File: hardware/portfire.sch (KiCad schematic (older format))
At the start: 31 parts, among them P101 1, P102 11, P103 2, P104 12, P105 3, P106 13, P107 4, P108 14, P109 5, P110 15, P111 6, P112 21, P113 7, P114 22, P115 8, P116 23, P117 9, P118 24, P119 10, P120 25, P121 16, P122 17, P123 18, P124 19, P125 20, P126 26, P127 27, P128 28, P129 29, P130 30

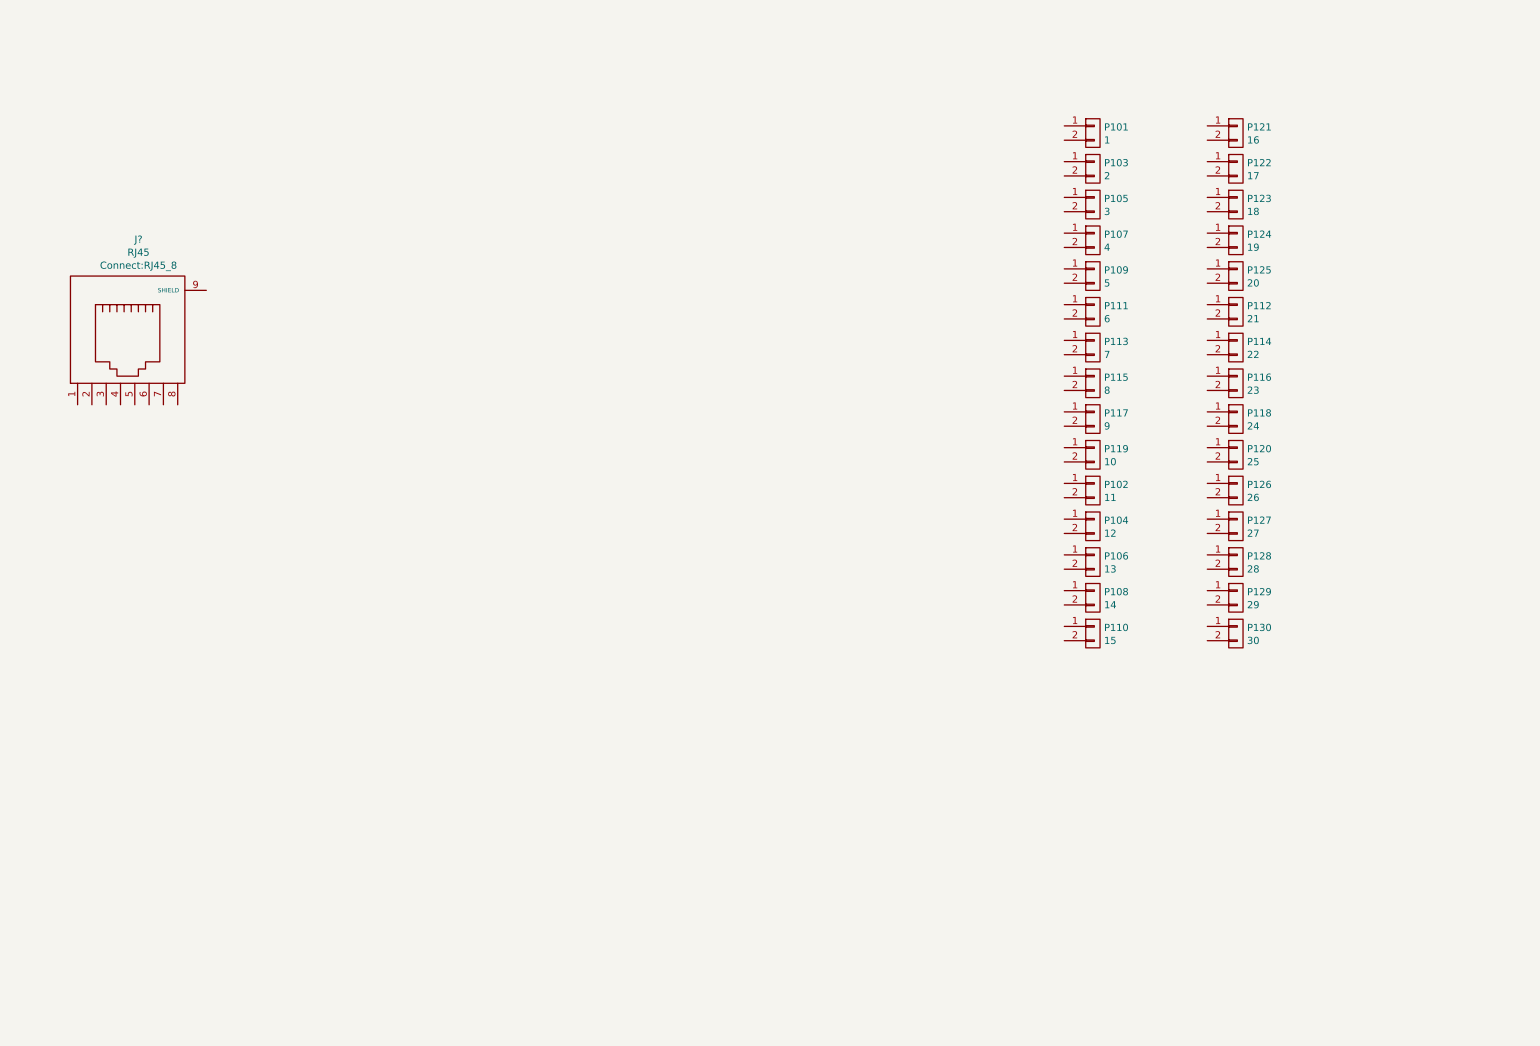
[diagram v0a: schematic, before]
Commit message: Roughed out ethernet part of schematic
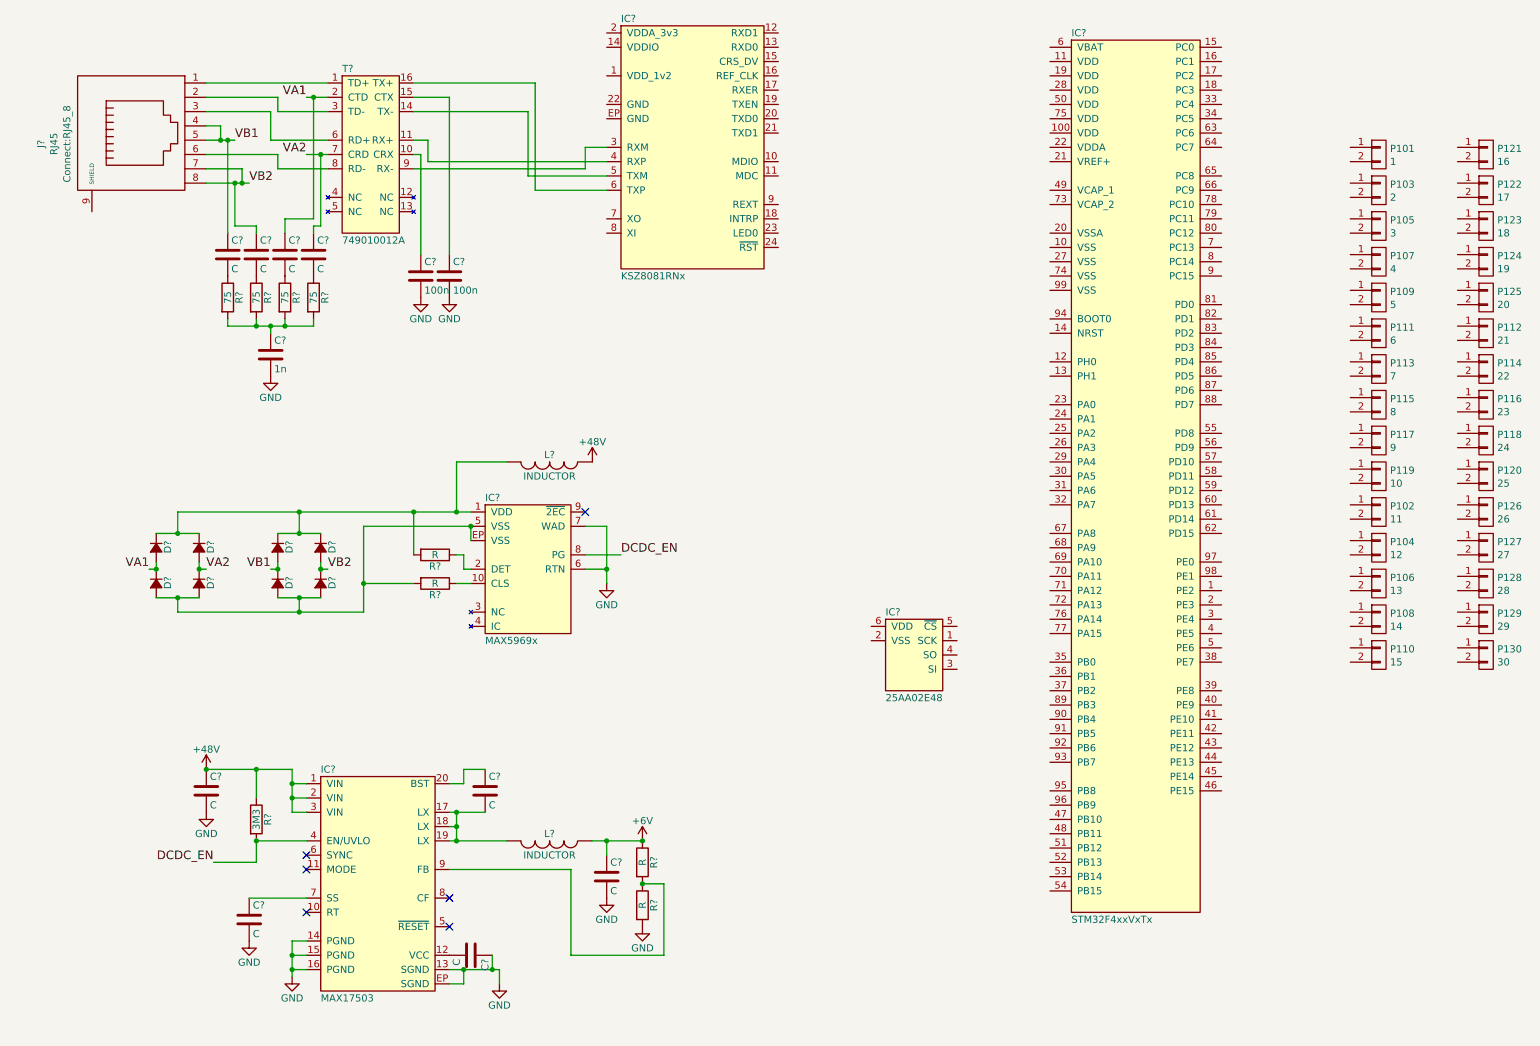
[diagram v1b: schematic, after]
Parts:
- added C? (x9): C, symbol C
- added C? (x2): 100n, symbol C
- added C?: 1n, symbol C
- added D? (x8): D_Small, symbol D_Small
- added IC?: MAX17503, agg:QFN-20-EP-MAX, symbol MAX17503
- added IC?: MAX5969x, agg:DFN-10-EP-MAX, symbol MAX5969x
- added IC?: STM32F4xxVxTx, agg:LQFP-100, symbol STM32F4xxVxTx
- added IC?: KSZ8081RNx, agg:QFN-24-EP-MICREL, symbol KSZ8081RNx
- added IC?: 25AA02E48, agg:SOT-23-6, symbol 25AA02E48
- added L? (x2): INDUCTOR, symbol INDUCTOR
- added R? (x4): R, symbol R
- added R?: 3M3, symbol R
- added R? (x4): 75, symbol R
- added T?: 749010012A, agg:749010012A, symbol 749010012A
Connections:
- net at J?.1: now also T?.1 (TD+)
- net at J?.2: now also T?.3 (TD-)
- net at J?.3: now also T?.6 (RD+)
- net VB1: now reaches J?.4
- net VB1: now also J?.5, C?.1, D?.1 (K), D?.2 (A)
- net at J?.6: now also T?.8 (RD-)
- net VB2: now reaches J?.7
- net VB2: now also J?.8, C?.1, D?.1 (K), D?.2 (A)
- new net: C?.2, IC?.12 (VCC)
- new net: C?.2, IC?.17 (LX), IC?.18 (LX), IC?.19 (LX), L?.2
- new net: C?.1, IC?.20 (BST)
- new net: C?.1, IC?.7 (SS)
- new net: IC?.9 (FB), R?.1, R?.2
- new net: D?.1 (K), D?.1 (K), D?.1 (K), D?.1 (K), IC?.1 (VDD), L?.2, R?.2
- new net: IC?.10 (CLS), R?.1
- new net: IC?.2 (DET), R?.1
- new net: D?.2 (A), D?.2 (A), D?.2 (A), D?.2 (A), IC?.5 (VSS), IC?.EP (VSS), R?.2
- new net: C?.1, T?.10 (CRX)
- new net: IC?.4 (RXP), T?.11 (RX+)
- new net: IC?.5 (TXM), T?.14 (TX-)
- new net: C?.1, T?.15 (CTX)
- new net: IC?.6 (TXP), T?.16 (TX+)
- new net: IC?.3 (RXM), T?.9 (RX-)
- new net: C?.2, R?.1 (x4)
- new net: C?.1, R?.2, R?.2, R?.2, R?.2
- new net +48V: C?.1, IC?.1 (VIN), IC?.2 (VIN), IC?.3 (VIN), L?.1, R?.1
- new net +6V: C?.1, L?.1, R?.1
- new net DCDC_EN: IC?.4 (EN/UVLO), IC?.8 (PG), R?.2
- new net GND: C?.1, C?.2, C?.2, C?.2, C?.2, C?.2, C?.2, IC?.13 (SGND), IC?.14 (PGND), IC?.15 (PGND), IC?.16 (PGND), IC?.6 (RTN), IC?.7 (WAD), IC?.EP (SGND), R?.2
- new net VA1: C?.1, D?.1 (K), D?.2 (A), T?.2 (CTD)
- new net VA2: C?.1, D?.1 (K), D?.2 (A), T?.7 (CRD)
- no-connect marks 0 -> 6
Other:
- moved on the sheet: J?, P101, P102, P103, P104, P105, P106, P107, P108, P109, P110, P111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

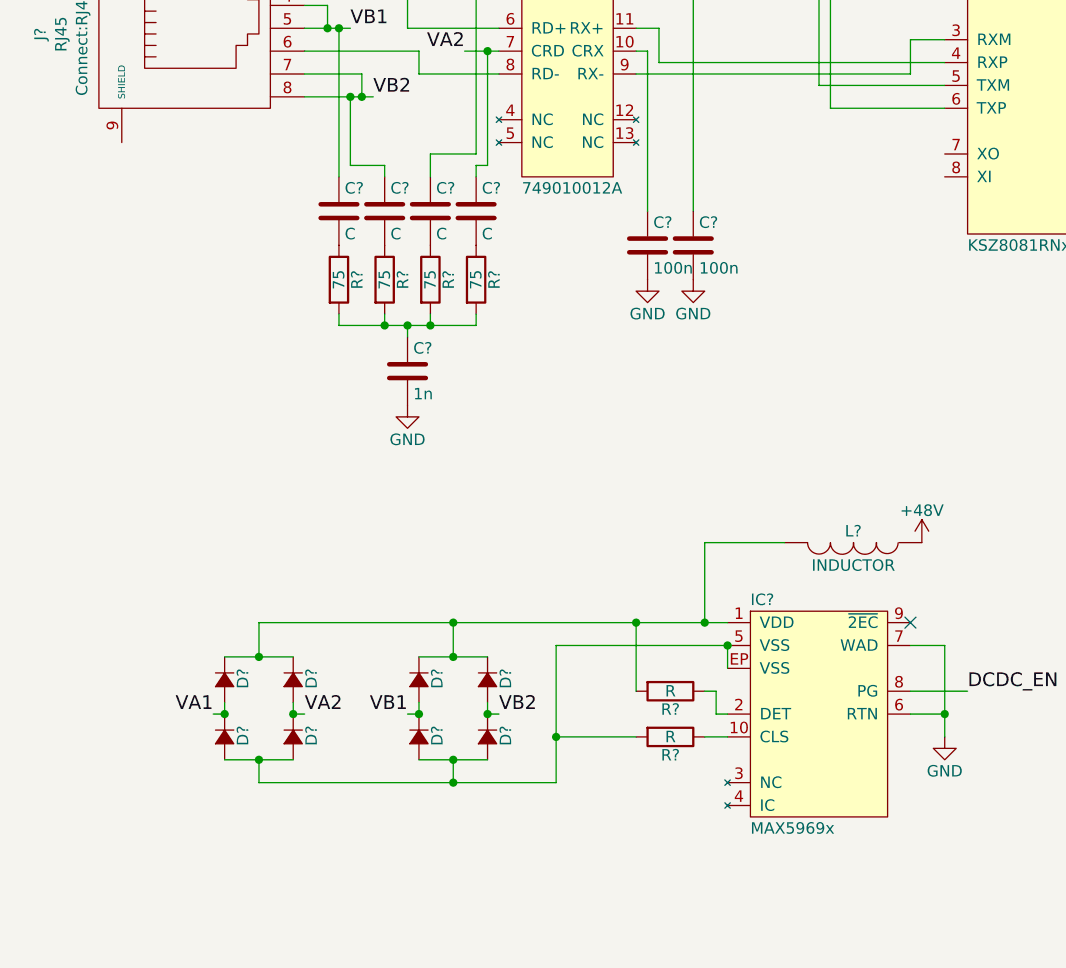
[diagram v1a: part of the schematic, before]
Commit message: Added lots of component specs around poe section
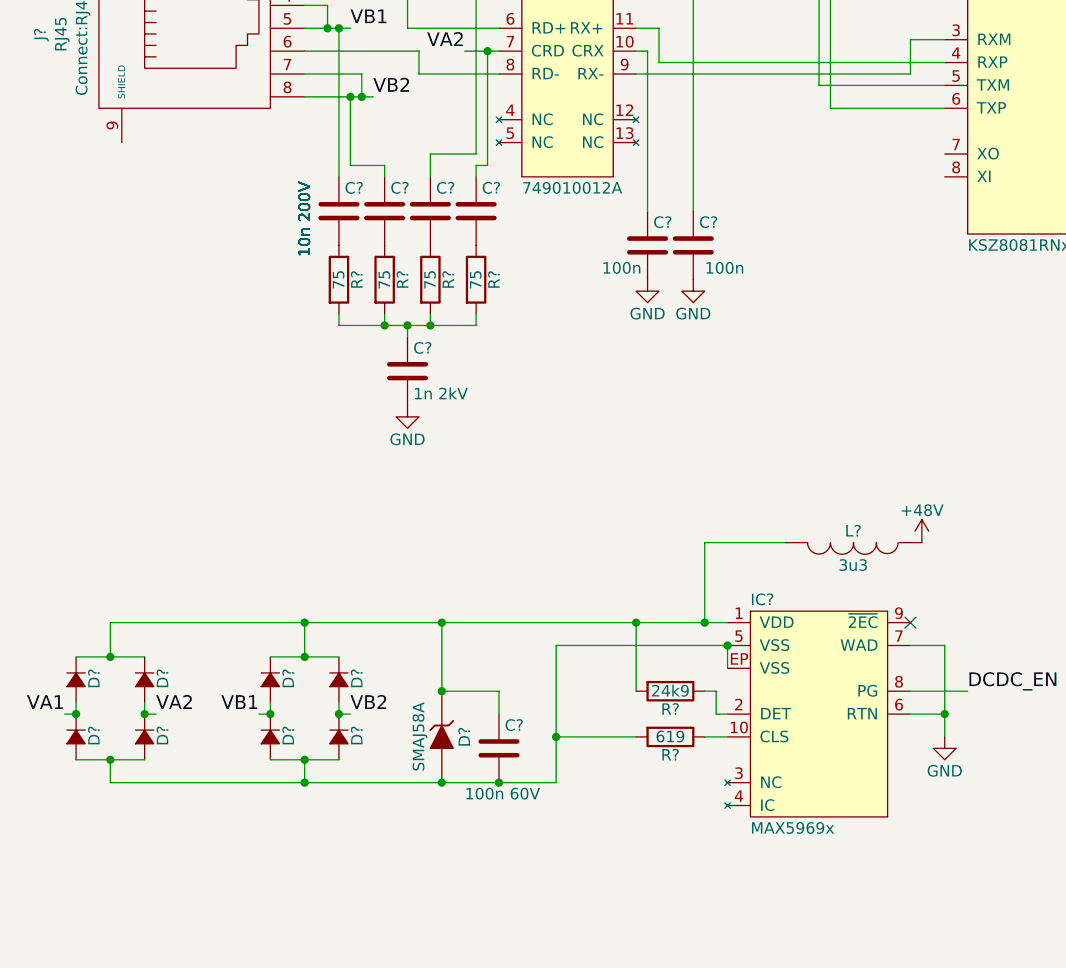
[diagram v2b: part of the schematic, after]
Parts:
- removed C?: 100n, symbol C
- removed C? (x3): C, symbol C
- removed D? (x7): D_Small, symbol D_Small
- removed R? (x3): 75, symbol R
- added C?: 100n 60V, agg-kicad:0805, symbol C
- added C? (x3): 10n 200V, agg-kicad:0805, symbol C
- added C?: 100n, agg-kicad:0603, symbol C
- added D? (x7): SS110B, agg-kicad:DO-214AA-SMB, symbol D_Small
- added D?: SMAJ58A, agg-kicad:DO-214AC-SMA, symbol ZENER
- added R? (x3): 75, agg-kicad:0603, symbol R
- C?: footprint (none) -> agg-kicad:0603; Farnell (none) -> 1650835
- C?: value C -> 10n 200V; footprint (none) -> agg-kicad:0805; Farnell (none) -> 1828955
- C?: value 1n -> 1n 2kV; footprint (none) -> agg-kicad:1206; Farnell (none) -> 2497062
- D?: value D_Small -> SS110B; footprint (none) -> agg-kicad:DO-214AA-SMB; Farnell (none) -> 1861422
- L?: value INDUCTOR -> 3u3; footprint (none) -> hardware:ELLATP3R3NB; Farnell (none) -> 1865686
- R?: value R -> 24k9; footprint (none) -> agg-kicad:0603; Farnell (none) -> 2059450
- R?: value R -> 619; footprint (none) -> agg-kicad:0603; Farnell (none) -> 2059317
- R?: footprint (none) -> agg-kicad:0603; Farnell (none) -> 2059571
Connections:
- net GND: now also C?.2
- net VA1: now also C?.1, D?.1 (K)
- net VA2: now also C?.1, D?.1 (K), D?.2 (A)
- net VB1: now also D?.1 (K), D?.2 (A)
- net VB2: now also C?.1, D?.1 (K), D?.2 (A)
- net at D?.1 (K), IC?.1 (VDD), L?.2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: now also C?.1, D?.1 (K), D?.1 (K), D?.1 (K), D?.1 (K)
- net at IC?.5 (VSS), IC?.EP (VSS), R?.2: now also C?.2, D?.2 (A), D?.2 (A), D?.2 (A), D?.2 (A), D?.2 (A)
- net at T?.15 (CTX): now also C?.1
- net at C?.1, R?.2: now also R?.2, R?.2, R?.2
- new net: C?.2, R?.1 (x3)
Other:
- moved on the sheet: D?
